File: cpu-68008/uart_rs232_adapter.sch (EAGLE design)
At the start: 19 parts, among them IC1 MAX232

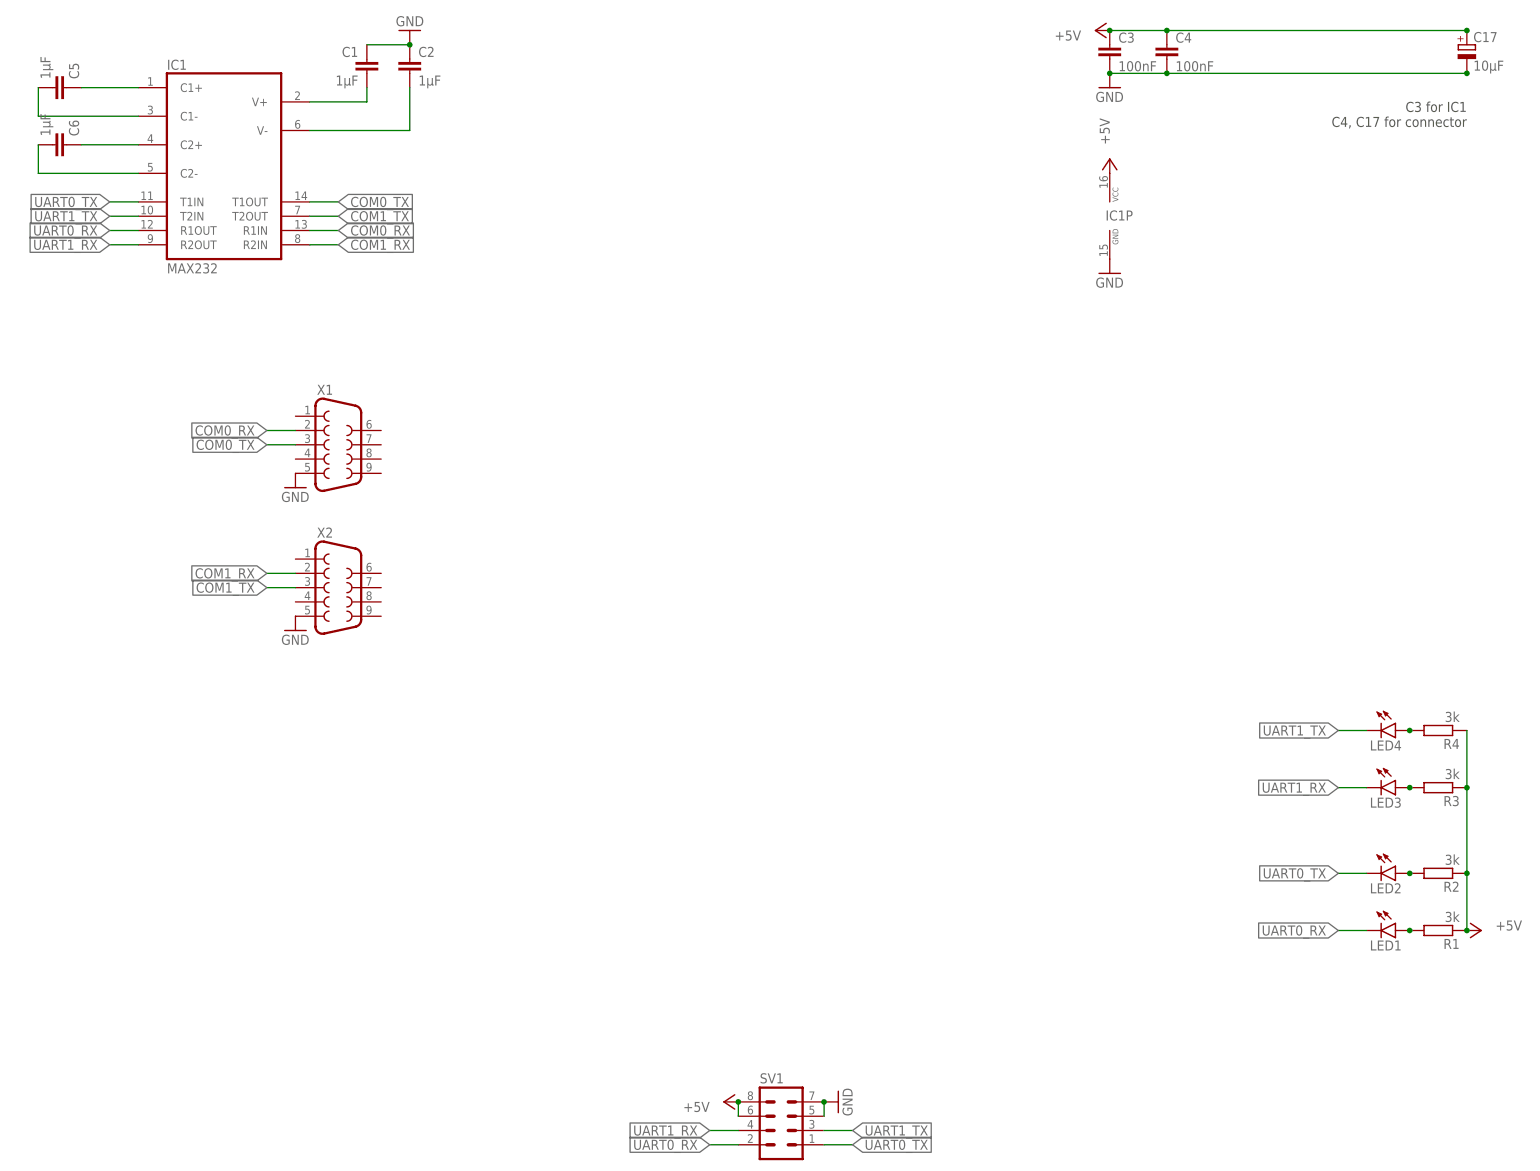
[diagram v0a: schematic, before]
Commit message: rev 01 boards for cpu-68008 sent to fab
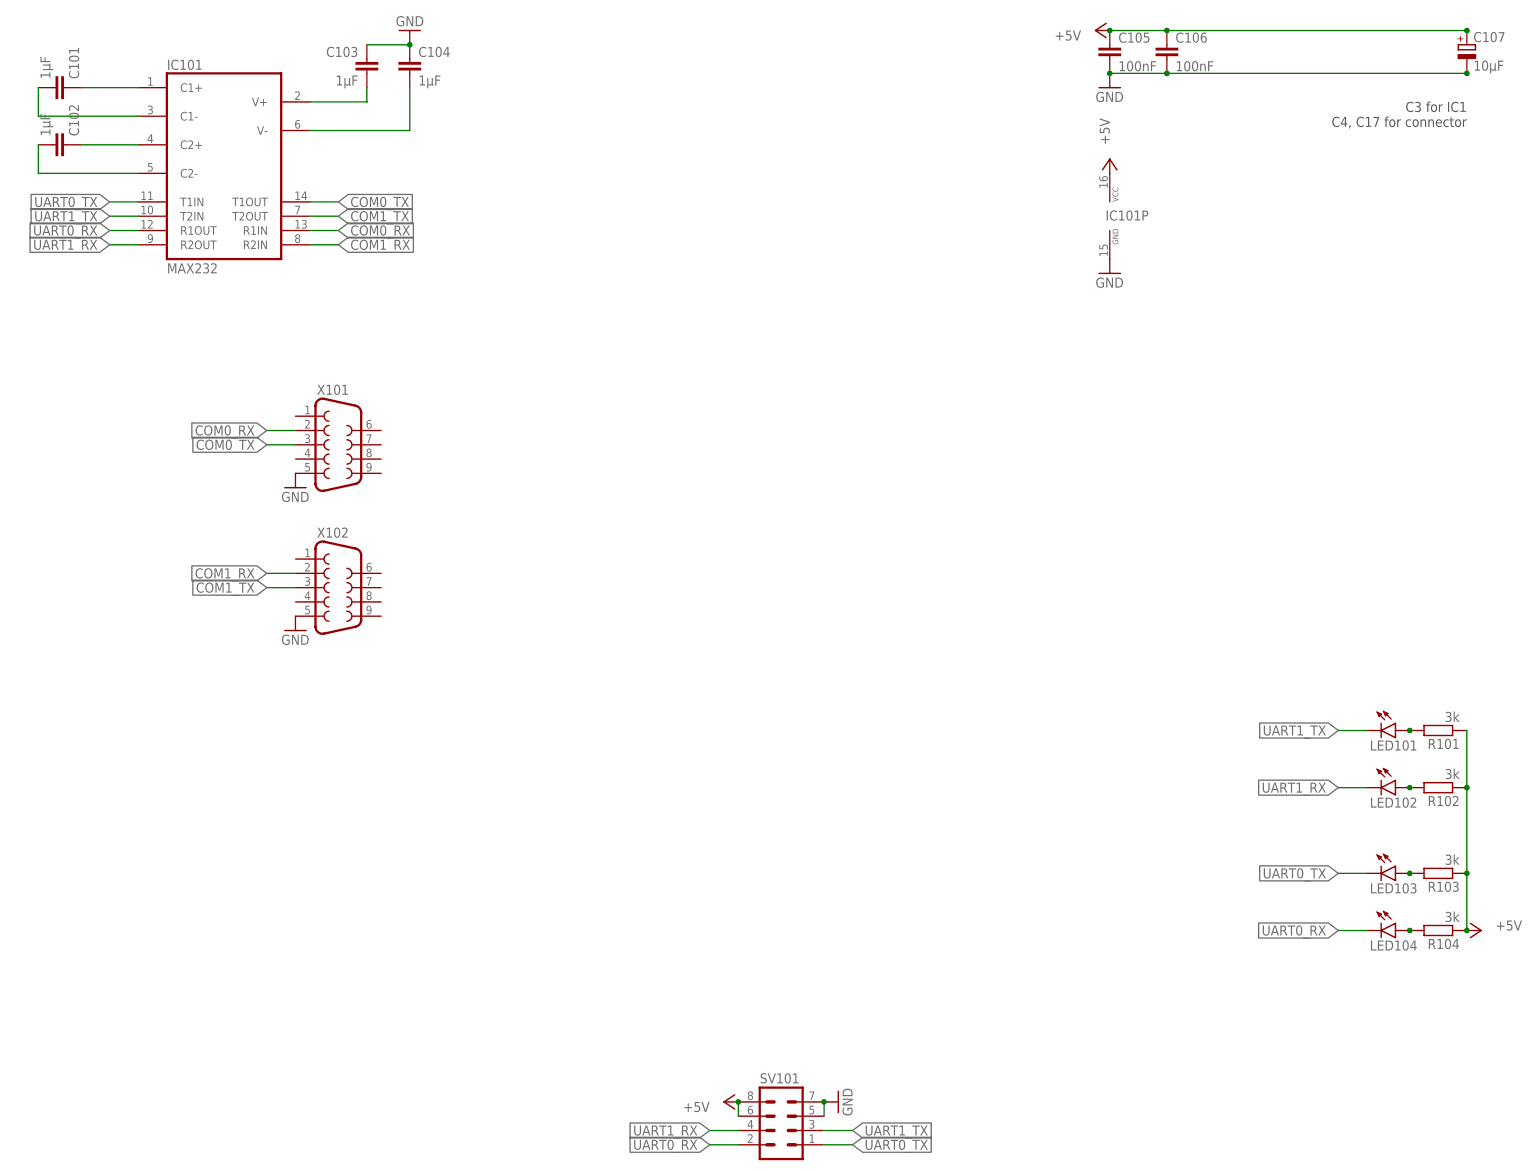
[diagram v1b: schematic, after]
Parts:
- IC101: MOUSER (none) -> 595-MAX232ECN
- renumbered C1 to C103, C17 to C107, C2 to C104, C3 to C105, C4 to C106, C5 to C101, C6 to C102, IC1 to IC101, LED1 to LED104, LED2 to LED103, LED3 to LED102, LED4 to LED101, R1 to R104, R2 to R103, R3 to R102, R4 to R101, SV1 to SV101, X1 to X101, X2 to X102
